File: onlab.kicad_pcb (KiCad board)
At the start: 2 copper layers, 100 x 100 mm, 86 parts, among them J1 Battery, J10 DC-Motor, J2 HC_SR04, J3 HC_SR04, J4 HC_SR04, J5 DC-Motor, J6 DC-Motor, J7 DC-Motor, J8 DC-Motor, J9 DC-Motor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

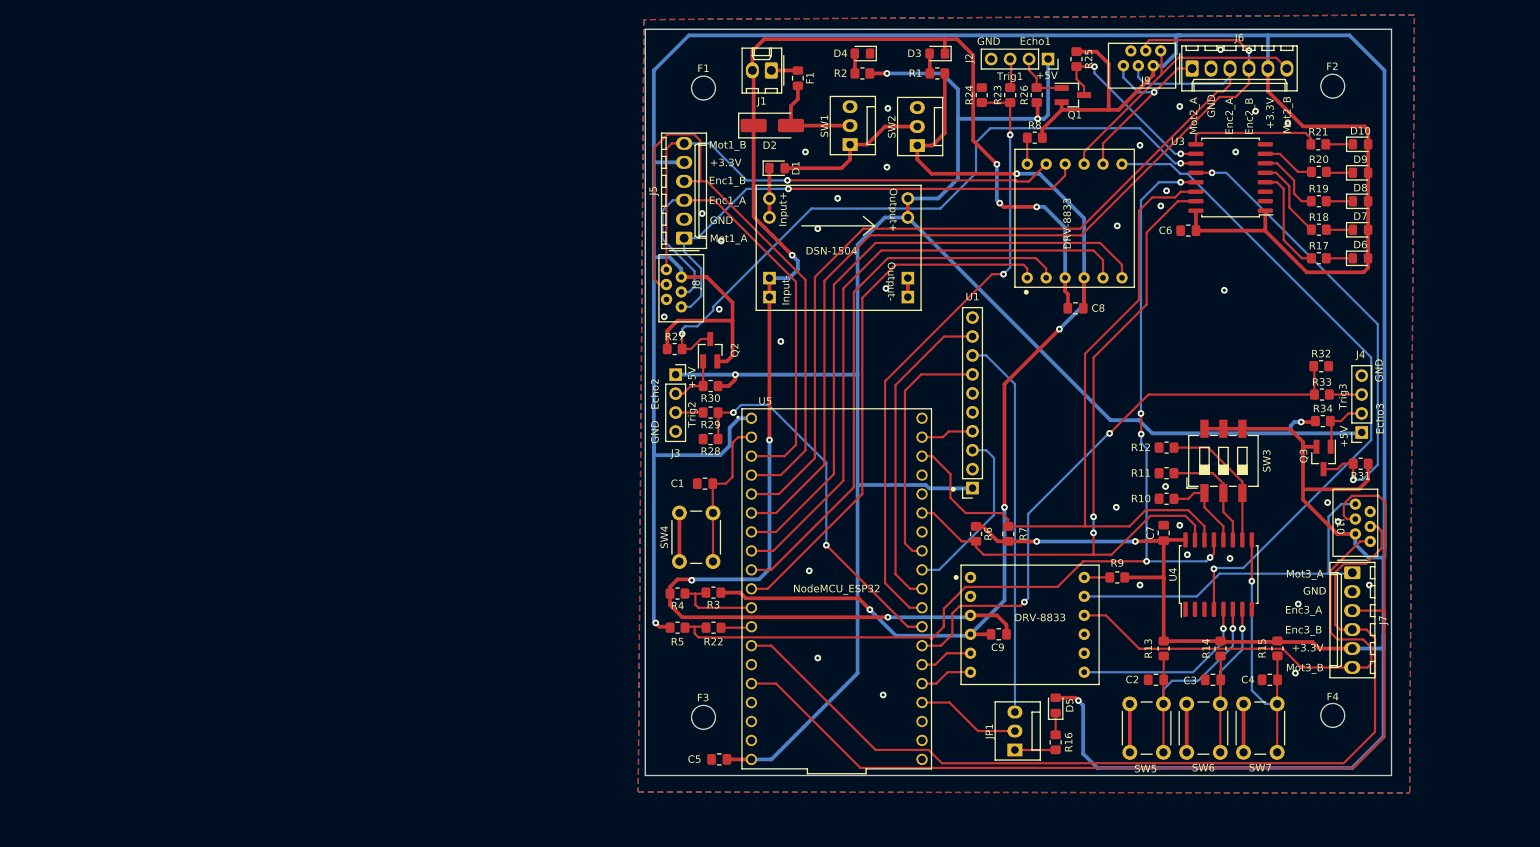
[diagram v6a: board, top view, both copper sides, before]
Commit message: Correction of schematic and layout
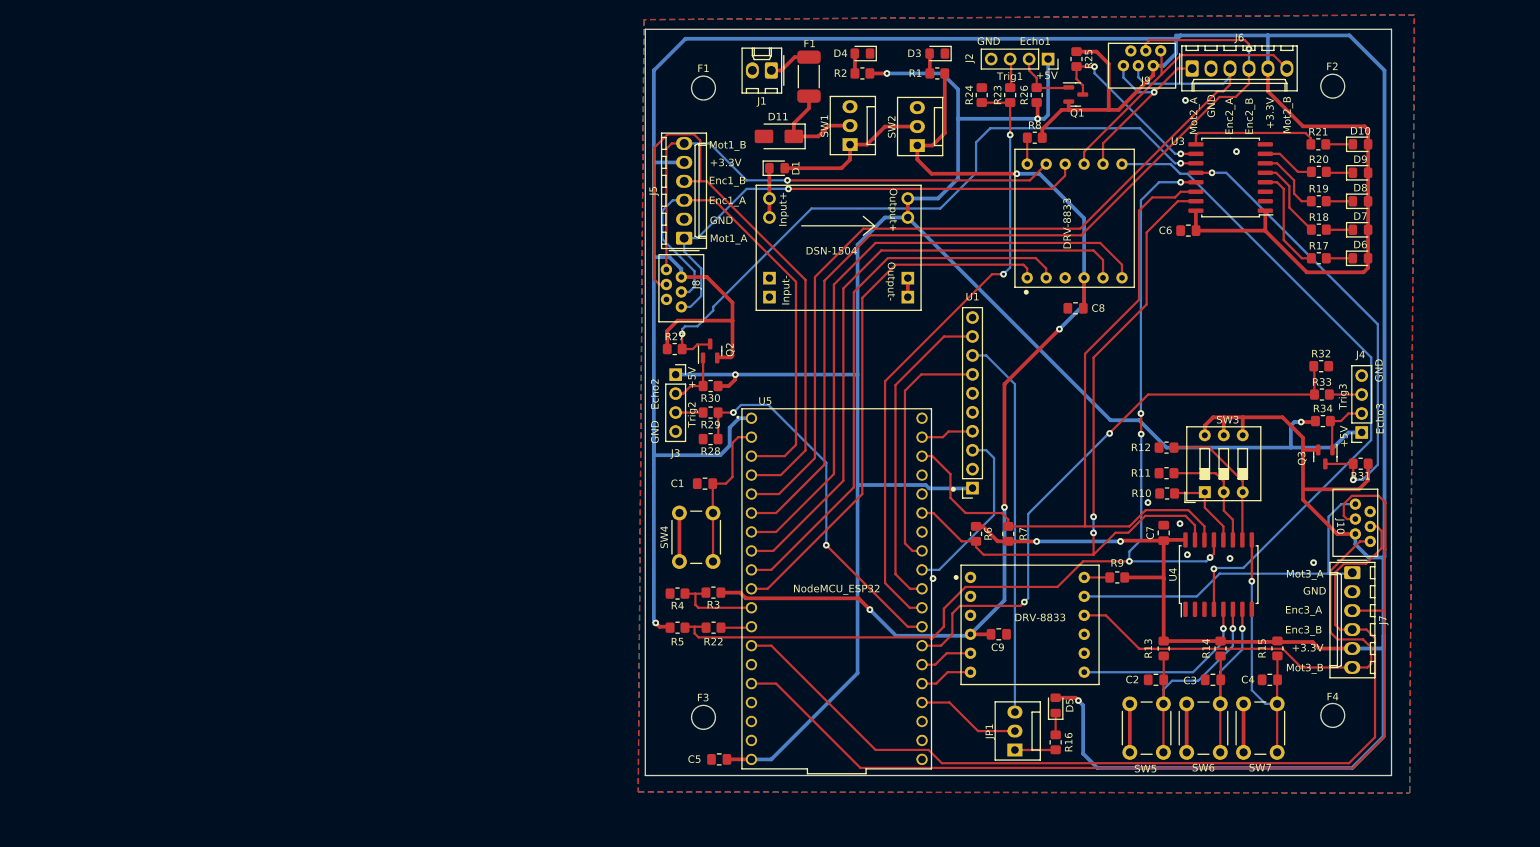
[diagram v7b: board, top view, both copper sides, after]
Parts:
- removed D2: D_TVS, Diode_SMD:D_SMA_Handsoldering
- added D11: SMAJ12A, Diode_SMD:D_SMA, F.Cu at (132.2, 41.4)
- C8, C9: value 0.1u -> 10u
- F1: value Polyfuse -> 1812L125/16; footprint Fuse:Fuse_0805_2012Metric_Pad1.15x1.40mm_HandSolder -> Onlab:polyfuse
- Q1, Q2, Q3: value NMOS -> 2N7002; footprint Package_TO_SOT_SMD:SOT-23_Handsoldering -> Package_TO_SOT_SMD:SOT-23
- R16, R17, R18, R19, R20, R21: value 67.5 -> 68
- SW3: footprint Button_Switch_SMD:SW_DIP_SPSTx03_Slide_6.7x9.18mm_W8.61mm_P2.54mm_LowProfile -> Button_Switch_THT:SW_DIP_SPSTx03_Slide_9.78x9.8mm_W7.62mm_P2.54mm
- moved SW3 4.87 mm to (189.3, 89.0)
- moved F1 4.81 mm to (137.8, 29.8)
- moved R10 0.72 mm to (184.2, 89.2)
- moved Q1 0.39 mm to (172.0, 35.7)
- moved Q3 0.28 mm to (205.4, 84.3)
- moved Q2 0.10 mm to (123.0, 70.1)
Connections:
- C8 pad 2: GNDPWR -> GND
- C9 pad 2: GNDPWR -> GND
- D3 pad 1: GNDPWR -> GND
- J1 pad 2: GNDPWR -> GND
- R4 pad 2: GNDPWR -> GND
- U2 pad 1: GNDPWR -> GND
- U6 pad 3: GNDPWR -> GND
- U7 pad 3: GNDPWR -> GND
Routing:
- net GNDPWR: track 215.3 -> 0.00 mm, vias 7 -> 0
- net +3.3V: track 618.6 -> 626.2 mm
- net +5V: track 265.8 -> 269.3 mm
- net +12V: track 3.56 -> 5.78 mm
- net Net-(J2-Pin_2): track 7.80 -> 8.67 mm
- net Net-(D11-A1): track 13.6 -> 14.4 mm
- net GND: track 28.5 -> 29.2 mm, vias 35 -> 8

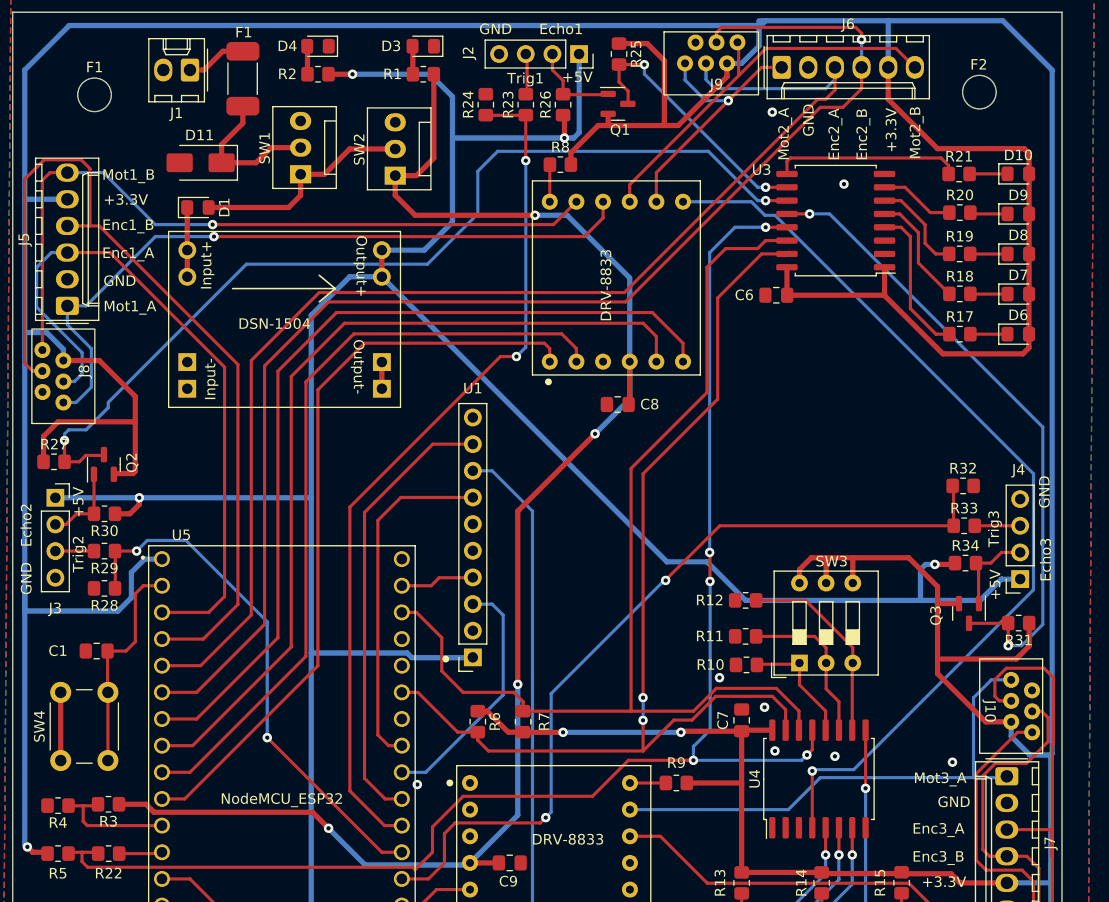
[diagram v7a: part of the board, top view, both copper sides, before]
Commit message: Correction of Q1, Q2, Q3 and update of libraries
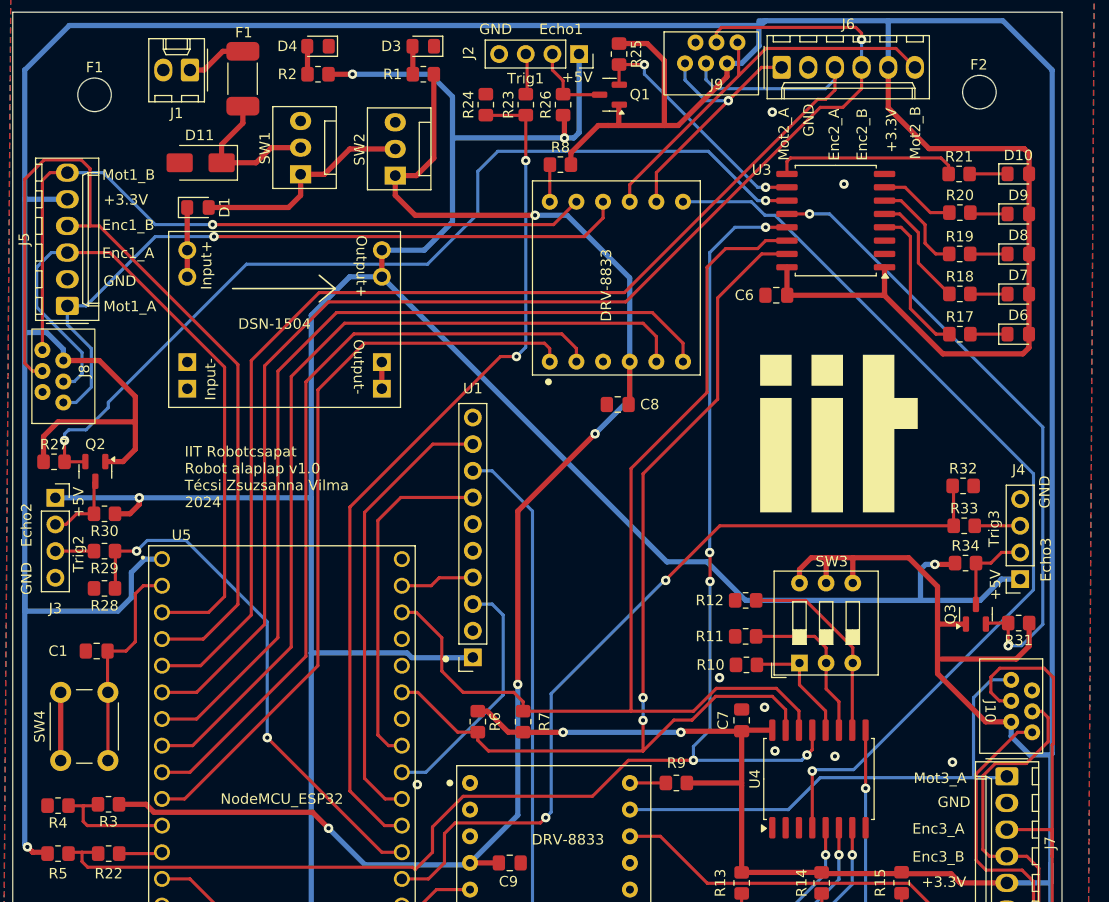
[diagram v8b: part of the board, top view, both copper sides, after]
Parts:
- added G***: LOGO, Onlab:IIT_logo_15x15mm, F.Cu at (193.0, 67.2)
- moved Q1 1.19 mm to (171.2, 34.9), turned to 180 degrees
- moved Q2 1.05 mm to (122.2, 70.8), turned to -90 degrees
- moved Q3 0.66 mm to (206.1, 84.4), turned to 90 degrees
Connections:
- Q1 pad 1: Net-(J2-Pin_2) -> +3.3V
- Q1 pad 2: +3.3V -> /UV_Trig_1
- Q1 pad 3: /UV_Trig_1 -> Net-(J2-Pin_2)
- Q2 pad 1: Net-(J3-Pin_2) -> +3.3V
- Q2 pad 2: +3.3V -> /UV_Trig_2
- Q2 pad 3: /UV_Trig_2 -> Net-(J3-Pin_2)
- Q3 pad 1: Net-(J4-Pin_2) -> +3.3V
- Q3 pad 2: +3.3V -> /UV_Trig_3
- Q3 pad 3: /UV_Trig_3 -> Net-(J4-Pin_2)
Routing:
- net /UV_Trig_1: track 25.7 -> 23.4 mm
- net /UV_Trig_2: track 91.7 -> 89.7 mm
- net /UV_Trig_3: track 61.9 -> 60.4 mm
- net +3.3V: track 626.2 -> 627.3 mm
- net Net-(J2-Pin_2): track 8.67 -> 7.75 mm
- net /Mot3_EncA: track 139.3 -> 139.9 mm
- net Net-(J3-Pin_2): track 7.87 -> 7.30 mm
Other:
- board text added: "IIT Robotcsapat Robot alaplap v1.0 Técsi Zsuzsanna Vilma 2024"
